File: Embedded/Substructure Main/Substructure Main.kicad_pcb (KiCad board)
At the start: 2 copper layers, 60 parts, among them J1 MicroSD, J2 C Pins, J3 Coin Cell, U1 G0 FFC, U10 LD1117S50TR_SOT223, U2 G1 FFC, U3 S FFC, U4 USB2513B_Bi, U5 MCP7940N-xMNY, U6 INA220AIDGSR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

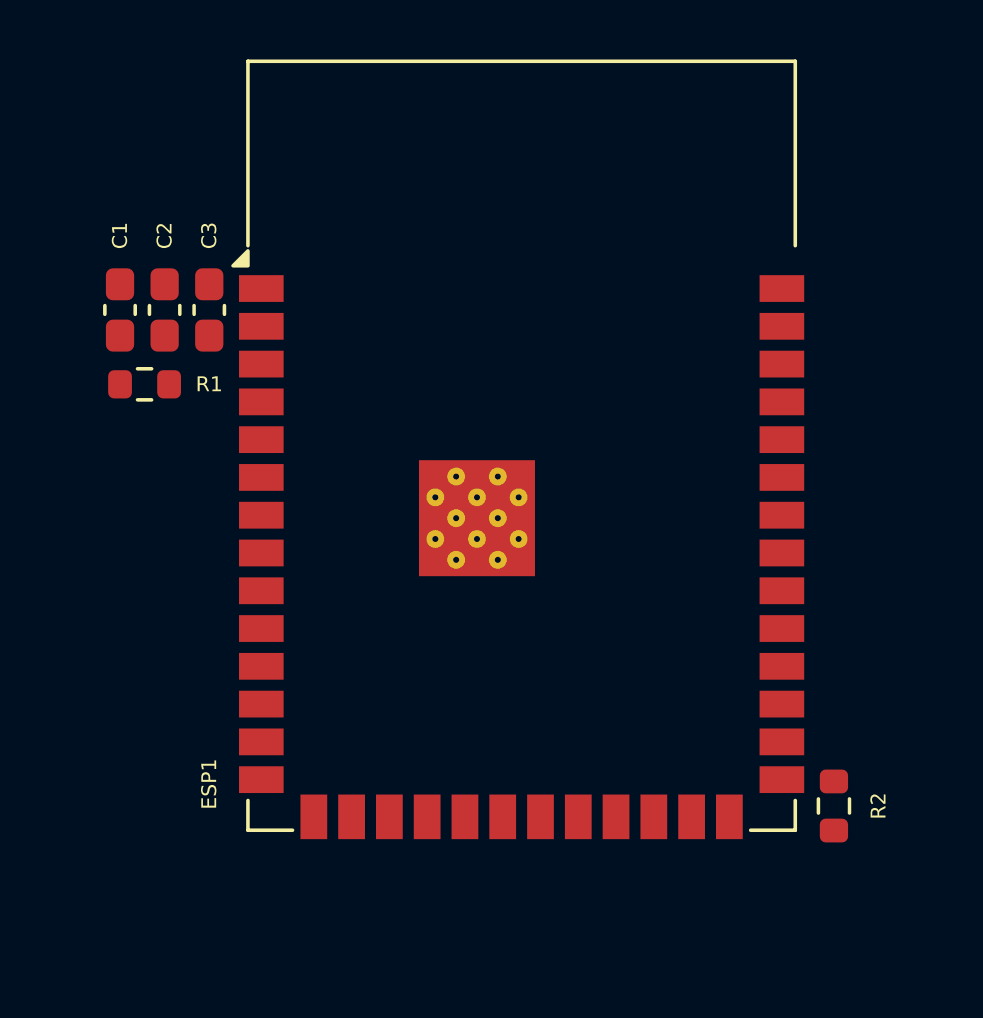
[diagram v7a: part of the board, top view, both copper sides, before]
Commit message: Modified ESP32 for 1U instead of Integrated Antenna
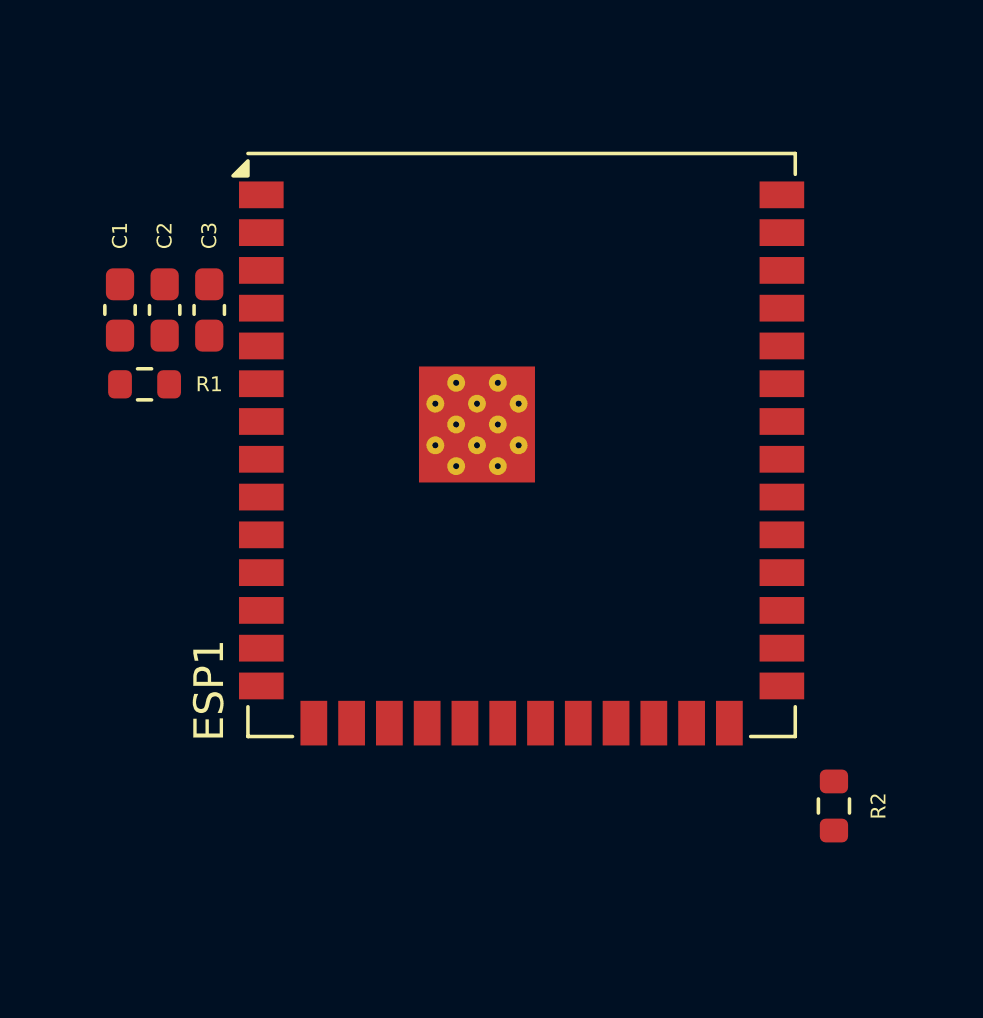
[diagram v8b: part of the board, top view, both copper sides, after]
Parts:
- ESP1: value ESP32-S3-WROOM-1 -> ESP32-S3-WROOM-1U; footprint RF_Module:ESP32-S3-WROOM-1 -> RF_Module:ESP32-S3-WROOM-1U
